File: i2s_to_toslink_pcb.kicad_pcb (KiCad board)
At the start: 2 copper layers, 61.5 x 61.7 mm, 66 parts, among them J1 PWR IN, J10 FCR684204T, J11 DIN_DOUT_2TP, J12 MCU_GPIOS1, J13 AJ_TP5, J14 C_G0, J15 C_G7, J16 C_RST, J17 C_CLKOUT, J2 EXT_CLK_IN5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

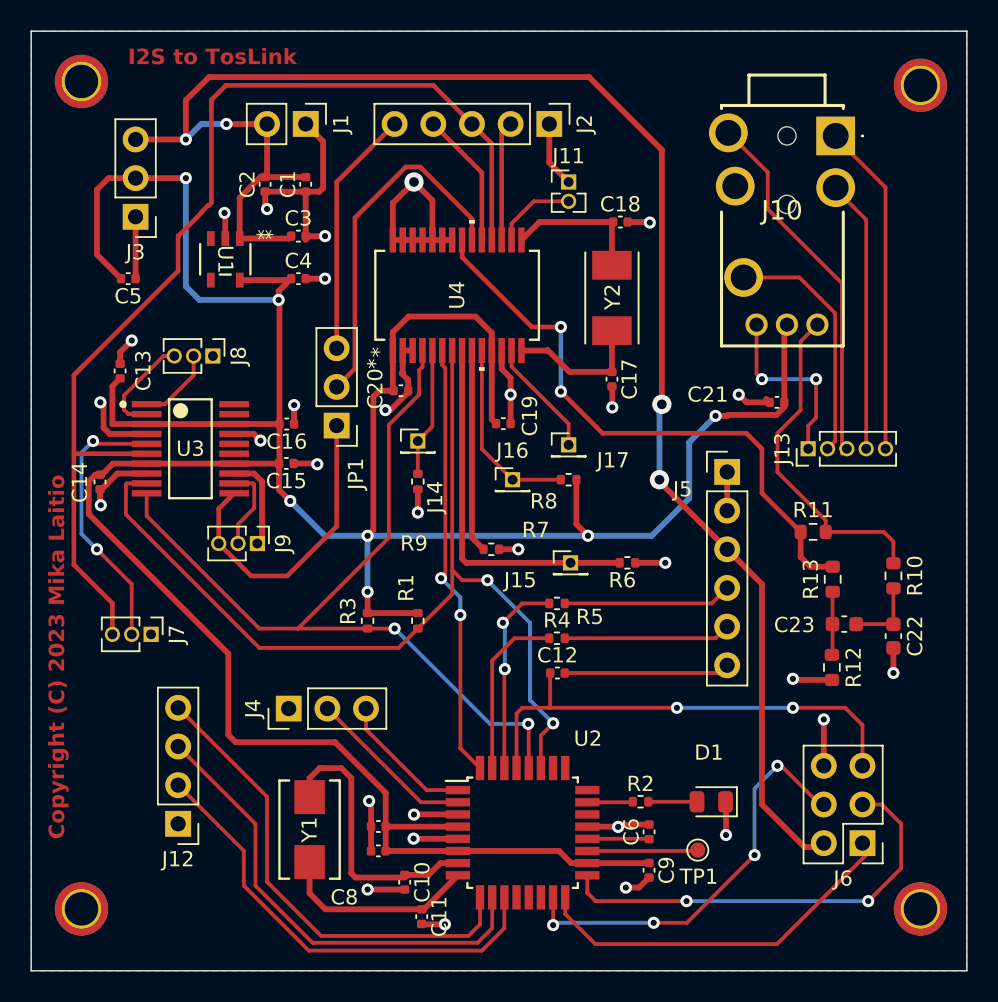
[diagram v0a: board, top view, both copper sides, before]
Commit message: small layout changes for some components
Signed-off-by: Mika Laitio <lamikr@gmail.com>
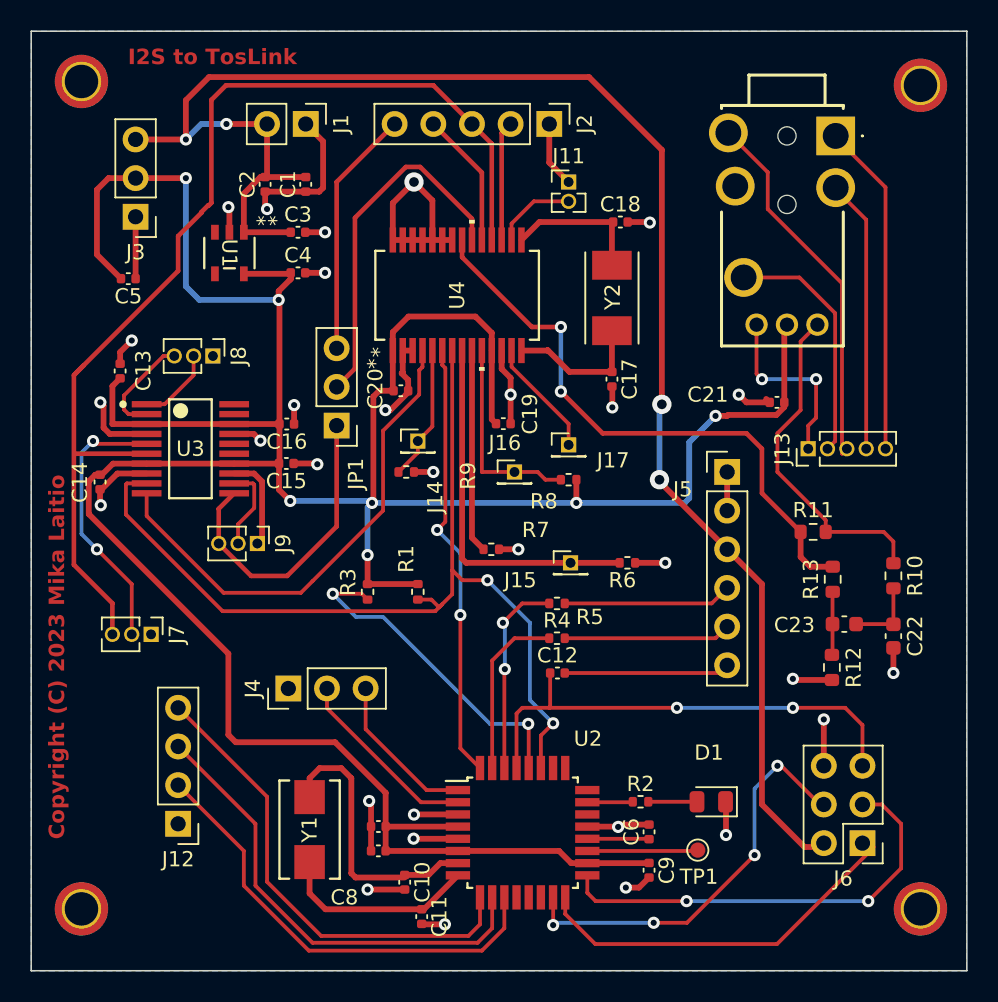
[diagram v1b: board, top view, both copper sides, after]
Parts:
- moved R1 1.90 mm to (46.2, 57.1)
- moved R3 1.90 mm to (42.9, 57.2)
- moved J4 1.32 mm to (37.7, 63.5)
- moved R9 0.99 mm to (45.5, 49.3), turned to 0 degrees
- moved J16 0.52 mm to (52.6, 49.3)
- moved U1 0.49 mm to (33.8, 34.9)
- moved C4 0.38 mm to (38.4, 36.2)
- moved C3 0.26 mm to (38.4, 33.5)
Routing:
- net VCC_3V3: track 215.9 -> 209.5 mm
- net GND: track 112.2 -> 108.7 mm
- net MCU_SCL1: track 56.8 -> 54.7 mm
- net Net-(J4-Pin_3): track 9.06 -> 10.4 mm
- net Net-(J4-Pin_2): track 11.1 -> 12.5 mm
- net VIN_5V: track 111.1 -> 110.3 mm

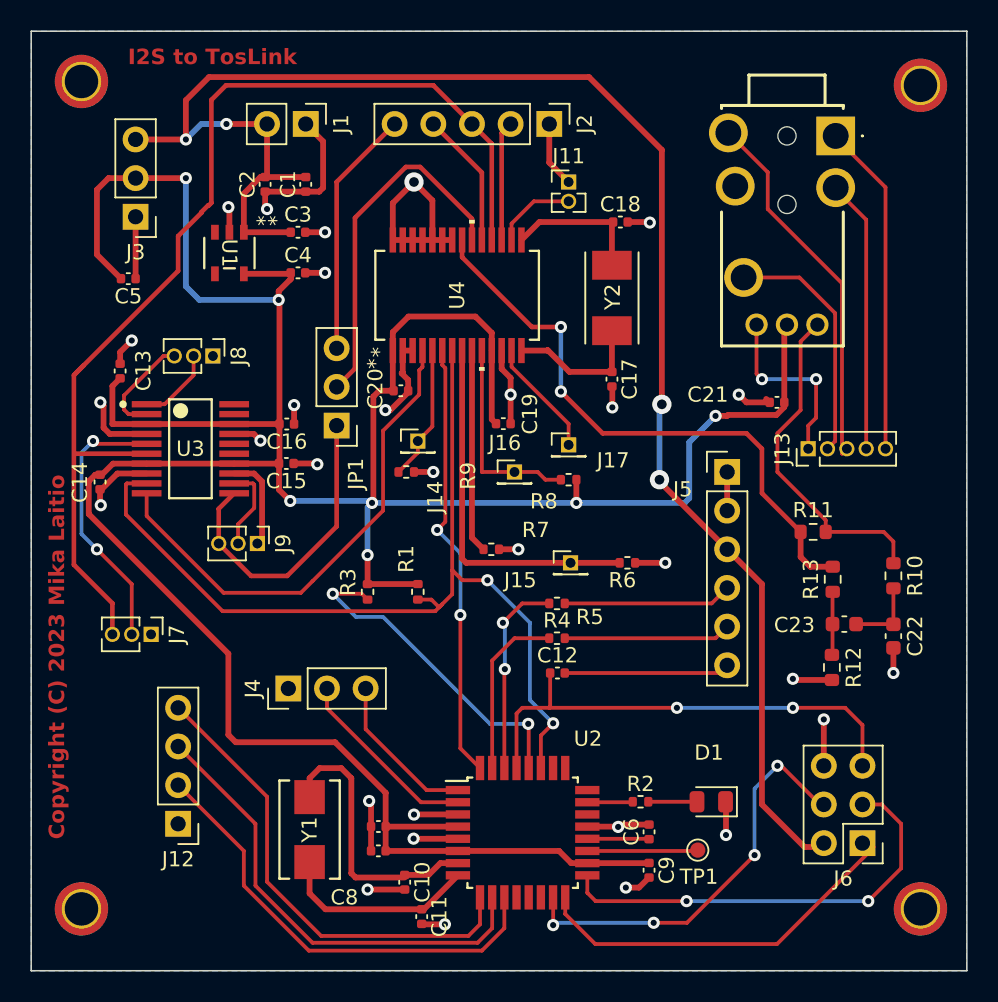
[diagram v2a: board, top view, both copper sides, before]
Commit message: cleaned up some vias not required
Signed-off-by: Mika Laitio <lamikr@gmail.com>
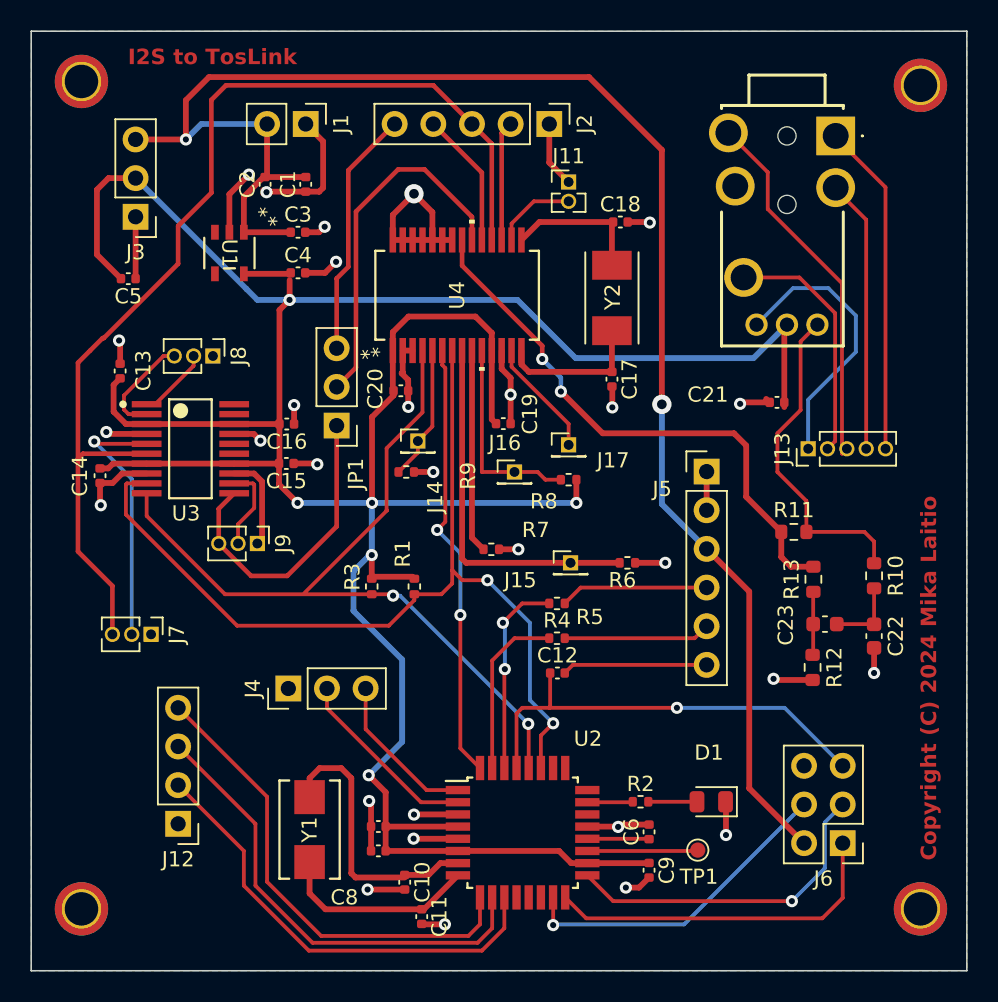
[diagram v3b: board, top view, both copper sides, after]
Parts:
- moved J5 1.35 mm to (65.2, 49.2)
- moved J6 1.30 mm to (74.1, 73.7)
- moved R13 1.27 mm to (72.2, 56.3)
- moved C22 1.27 mm to (76.2, 60.1)
- moved C23 1.27 mm to (73.0, 59.3)
- moved R10 1.27 mm to (76.2, 56.1)
- moved R11 1.27 mm to (70.9, 53.2)
- moved R12 1.27 mm to (72.2, 62.1)
- moved R3 0.45 mm to (43.2, 56.8)
- moved R1 0.42 mm to (46.0, 56.8)
- moved C14 0.42 mm to (25.3, 49.5)
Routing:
- net MCU_SCK: track 28.9 -> 21.9 mm, vias 2 -> 1
- net Net-(J10-GND_2): track 12.1 -> 18.3 mm, vias 2 -> 0
- net MCU_MOSI: track 27.7 -> 21.8 mm, vias 4 -> 1
- net GND: track 108.7 -> 103.5 mm, vias 30 -> 29
- net VCC_3V3: track 209.5 -> 205.7 mm, vias 7 -> 6
- net MCU_RST: track 31.9 -> 29.1 mm, vias 2 -> 1
- net CODEC_OUT_SPDIF_AUDIO_DATA: track 39.1 -> 36.9 mm
- net MCU_MISO: track 24.8 -> 23.0 mm
- net VIN_5V: track 110.3 -> 108.7 mm, vias 4 -> 2
- net Net-(J5-Pin_6): track 10.9 -> 9.54 mm
- net Net-(J5-Pin_5): track 11.0 -> 9.65 mm
- net Net-(J5-Pin_4): track 11.1 -> 9.75 mm
- net MCU_SDA1: track 62.8 -> 61.5 mm
- net EXTERNAL_IN_I2S_BCLK: track 72.1 -> 71.1 mm
- net Net-(J7-Pin_2): track 18.1 -> 17.3 mm, vias 2 -> 1
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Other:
- board text added: "Copyright (C) 2024 Mika Laitio"
- board text removed: "Copyright (C) 2023 Mika Laitio"

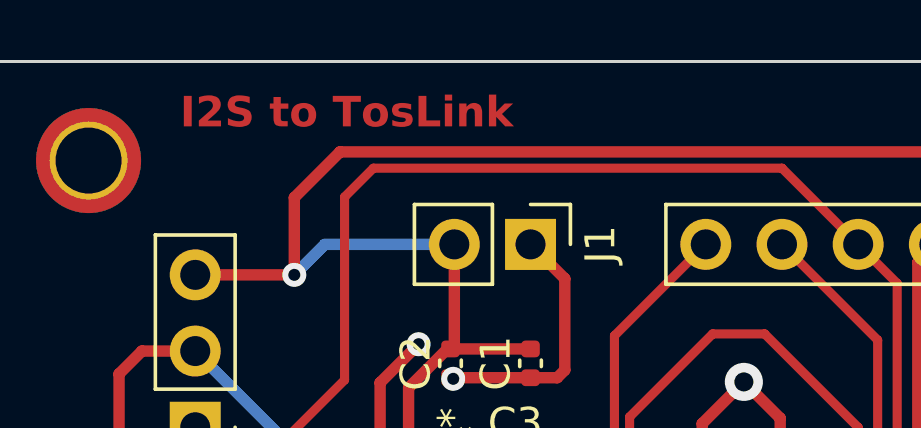
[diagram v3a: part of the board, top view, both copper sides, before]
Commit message: added version label v0.1 to pcb
Signed-off-by: Mika Laitio <lamikr@gmail.com>
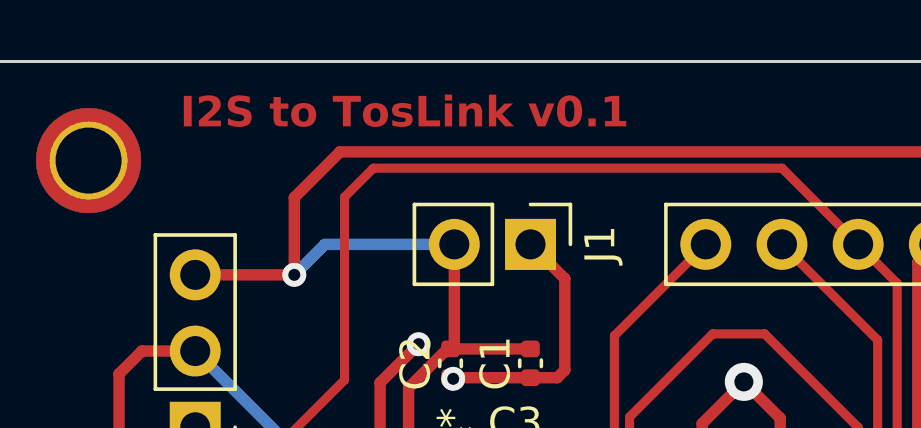
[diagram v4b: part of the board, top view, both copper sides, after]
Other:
- board text added: "I2S to TosLink v0.1"
- board text removed: "I2S to TosLink"
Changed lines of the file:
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@@
         (effects (font (size 1 1) (thickness 0.15)))
     )
-    (fp_text value "EXT_CLK_IN5" (at -4.318 10.922 -180) (layer "F.Fab")
+    (fp_text value "EXT_CLK_IN5" (at -4.318 6.464 -180) (layer "F.Fab")
         (effects (font (size 1 1) (thickness 0.15)))
     )
@@
   (gr_rect (start 20.828 20.32) (end 82.296 82.042)
     (stroke (width 0.1) (type default)) (fill none) (layer "Edge.Cuts"))
-  (gr_text "I2S to TosLink" (at 27.178 22.606) (layer "F.Cu")
+  (gr_text "I2S to TosLink v0.1" (at 27.178 22.606) (layer "F.Cu")
     (effects (font (size 1.016 1.016) (thickness 0.2032) bold) (justify left bottom))
   )
